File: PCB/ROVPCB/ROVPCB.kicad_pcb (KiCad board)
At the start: 2 copper layers, 65 x 56 mm, 17 parts, among them J1 Conn_01x04_Male, J2 Conn_01x04_Male, J3 Conn_Coaxial, P1 Conn_02x20_Odd_Even, U1 MPU-9250, U2 BME280, U3 LIGHT_TSL2591, U4 LTC4316IDDPBF, U5 AtlasOEM

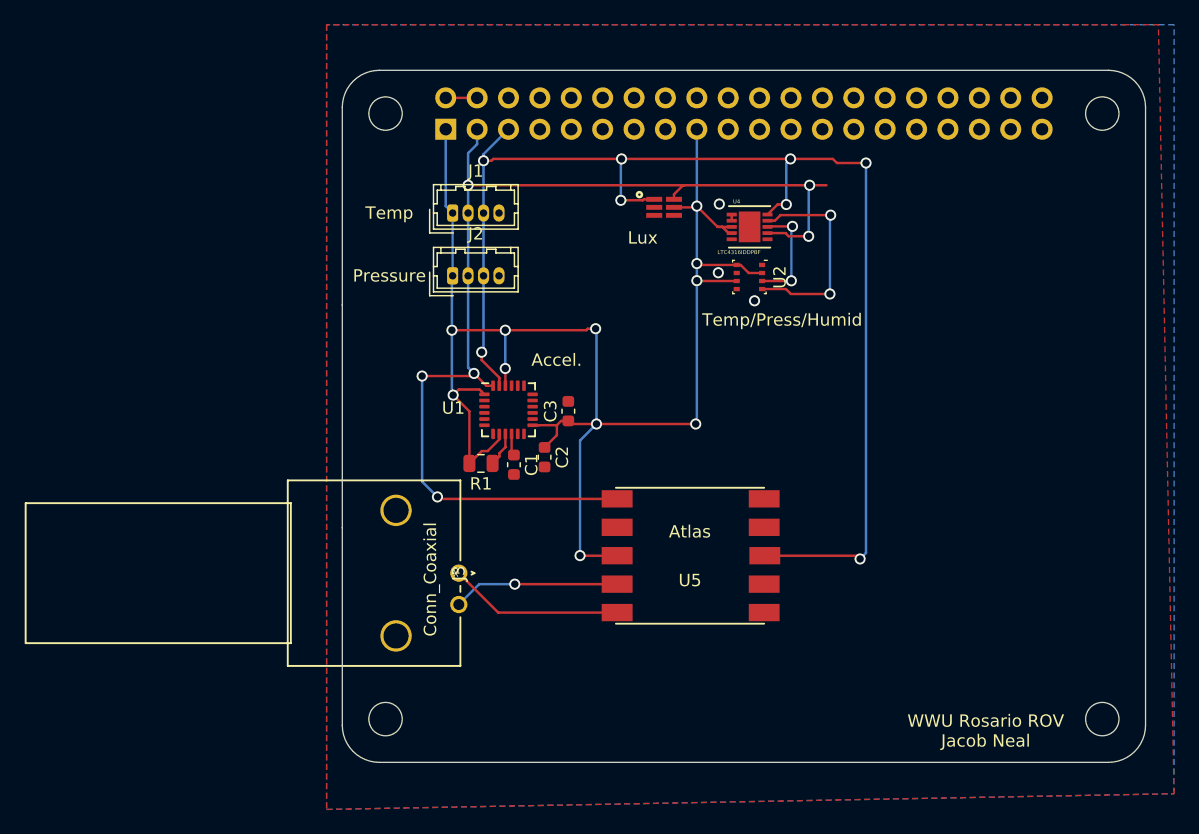
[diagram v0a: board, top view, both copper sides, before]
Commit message: NO BNC! YASSS
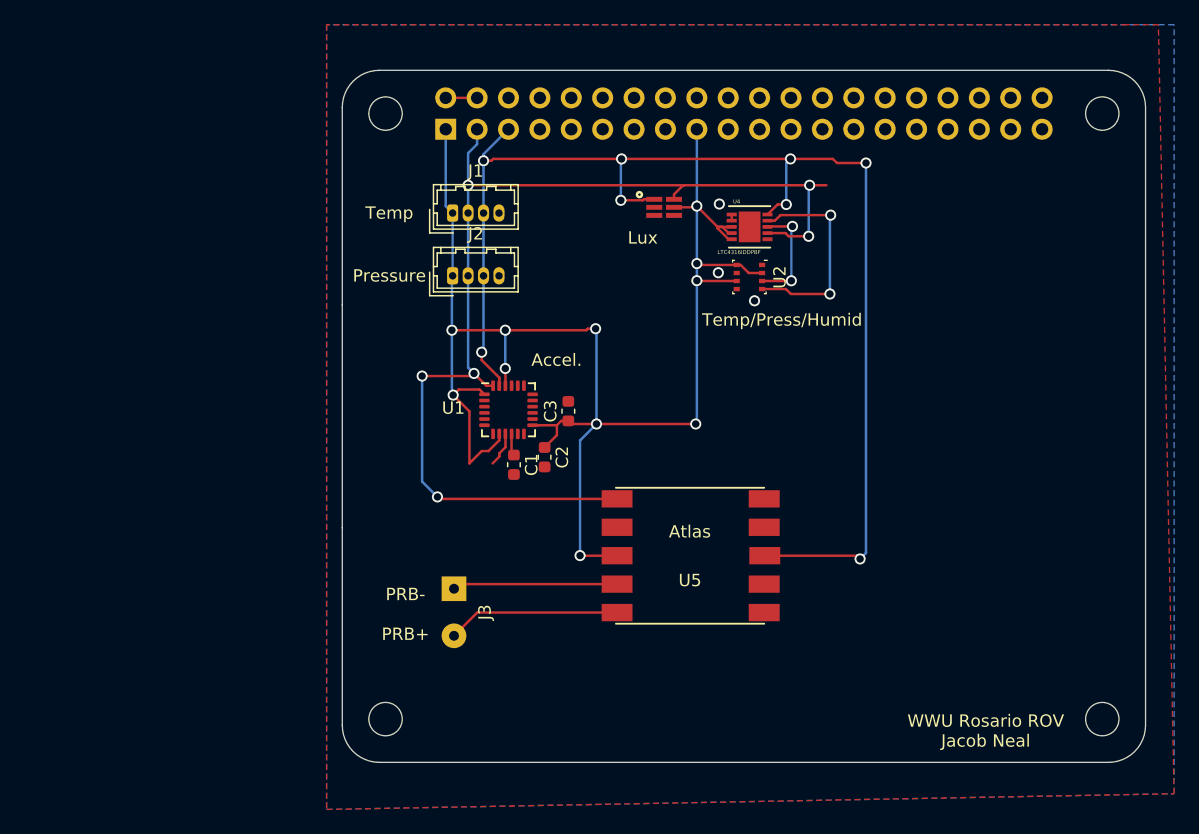
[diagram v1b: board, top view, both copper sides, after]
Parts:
- removed R1: 10k, Resistor_SMD:R_0805_2012Metric
- J3: value Conn_Coaxial -> Conn_01x02_Male; footprint footprints:5227161-1 -> Connector_Wire:SolderWirePad_1x02_P3.81mm_Drill0.8mm
- moved J3 1.32 mm to (209.0, 135.9), turned to 270 degrees
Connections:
- U1 pad 9: Net-(R1-Pad1) -> GND
- U4 pad 5: Net-(U4-Pad5) -> +3V3
- U5 pad 4: Net-(J3-Pad2) -> Net-(J3-Pad1)
- U5 pad 5: Net-(J3-Pad1) -> Net-(J3-Pad2)
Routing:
- net Net-(R1-Pad1): track 2.82 -> 0.00 mm
- net GND: track 0.50 -> 3.32 mm
- net +3V3: track 128.5 -> 130.1 mm
- net Net-(J3-Pad1): track 14.1 -> 13.4 mm
- net Net-(J3-Pad2): track 13.5 -> 14.0 mm, vias 1 -> 0
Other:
- board text added: "PRB- PRB+"

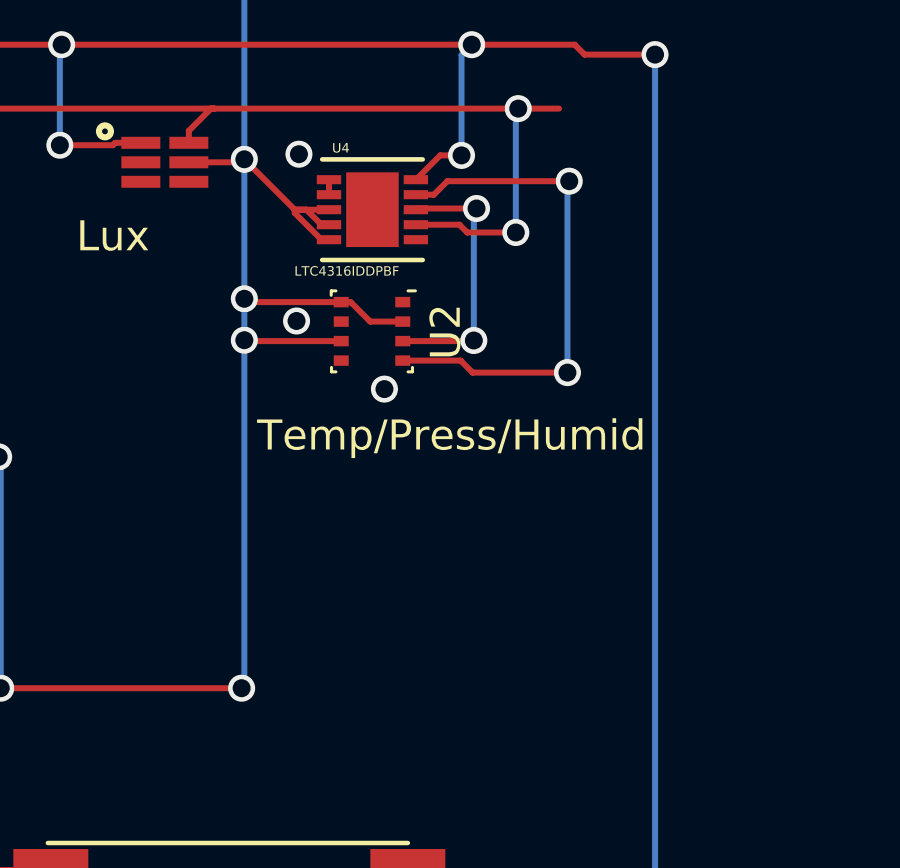
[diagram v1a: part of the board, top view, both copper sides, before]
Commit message: Pullup resistors in between translater and humidity sensor
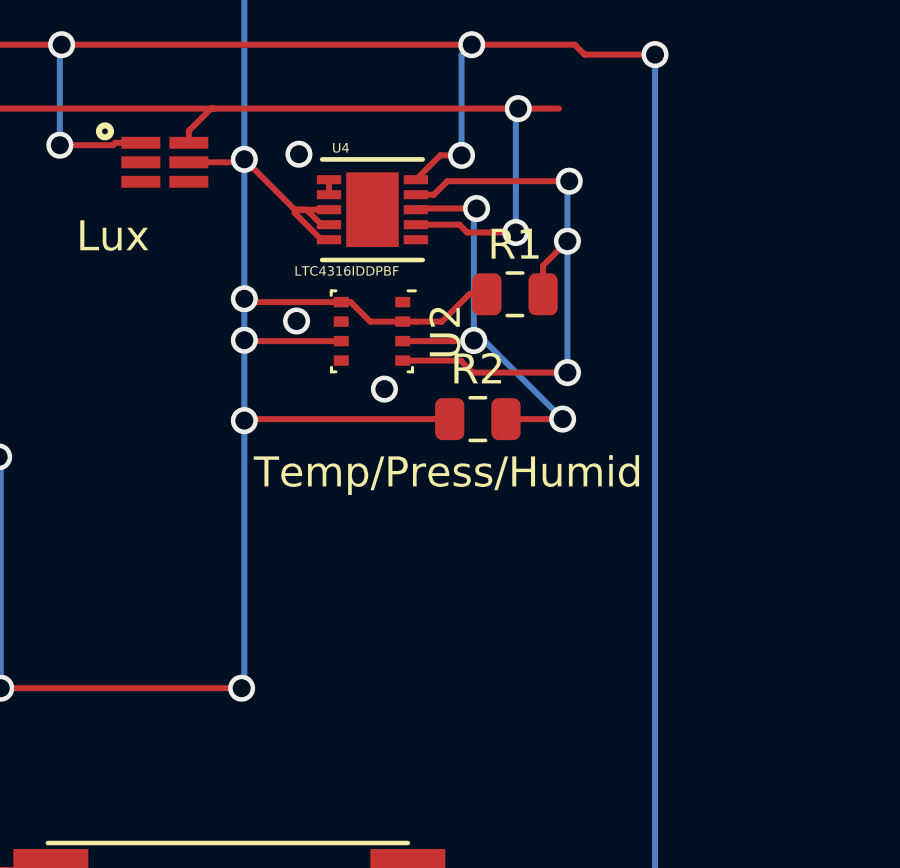
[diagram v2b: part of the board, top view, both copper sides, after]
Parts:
- added R1: 3k, Resistor_SMD:R_0805_2012Metric, F.Cu at (237.7, 109.5)
- added R2: 3k, Resistor_SMD:R_0805_2012Metric, F.Cu at (236.5, 113.7)
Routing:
- net +3V3: track 130.1 -> 140.2 mm, vias 11 -> 12
- net Net-(R2-Pad2): track 8.85 -> 14.8 mm, vias 2 -> 3
- net Net-(R1-Pad2): track 17.4 -> 19.5 mm, vias 2 -> 3

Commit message: I dont have time
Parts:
- added C4: 10uF, Capacitor_SMD:C_0603_1608Metric, F.Cu at (254.2, 113.7)
- added C5: 0.1uF, Capacitor_SMD:C_0603_1608Metric, F.Cu at (258.0, 110.1)
- added C6: 0.1uF, Capacitor_SMD:C_0603_1608Metric, F.Cu at (257.2, 113.2)
- added J4: Conn_01x01_Male, Connector_Wire:SolderWirePad_1x01_Drill0.8mm, F.Cu at (255.0, 110.9)
- added R3: 1k, Resistor_SMD:R_0805_2012Metric, F.Cu at (251.0, 113.9)
- added U6: LTC2451CTS8-TRMPBF, footprints:LTC2451CTS8-TRMPBF, F.Cu at (251.4, 111.1)
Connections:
- U5 pad 1: /GPIO2(SDA1) -> Net-(U5-Pad1)
- U5 pad 10: Net-(U5-Pad10) -> Net-(J3-Pad1)
- U5 pad 2: Net-(U5-Pad2) -> /GPIO3(SCL1)
- U5 pad 3: +3V3 -> Net-(U5-Pad3)
- U5 pad 4: Net-(J3-Pad1) -> Net-(U5-Pad4)
- U5 pad 5: Net-(J3-Pad2) -> Net-(U5-Pad5)
- U5 pad 6: GND -> Net-(U5-Pad6)
- U5 pad 7: Net-(U5-Pad7) -> /GPIO2(SDA1)
- U5 pad 8: /GPIO3(SCL1) -> Net-(U5-Pad8)
- U5 pad 9: Net-(U5-Pad9) -> +3V3

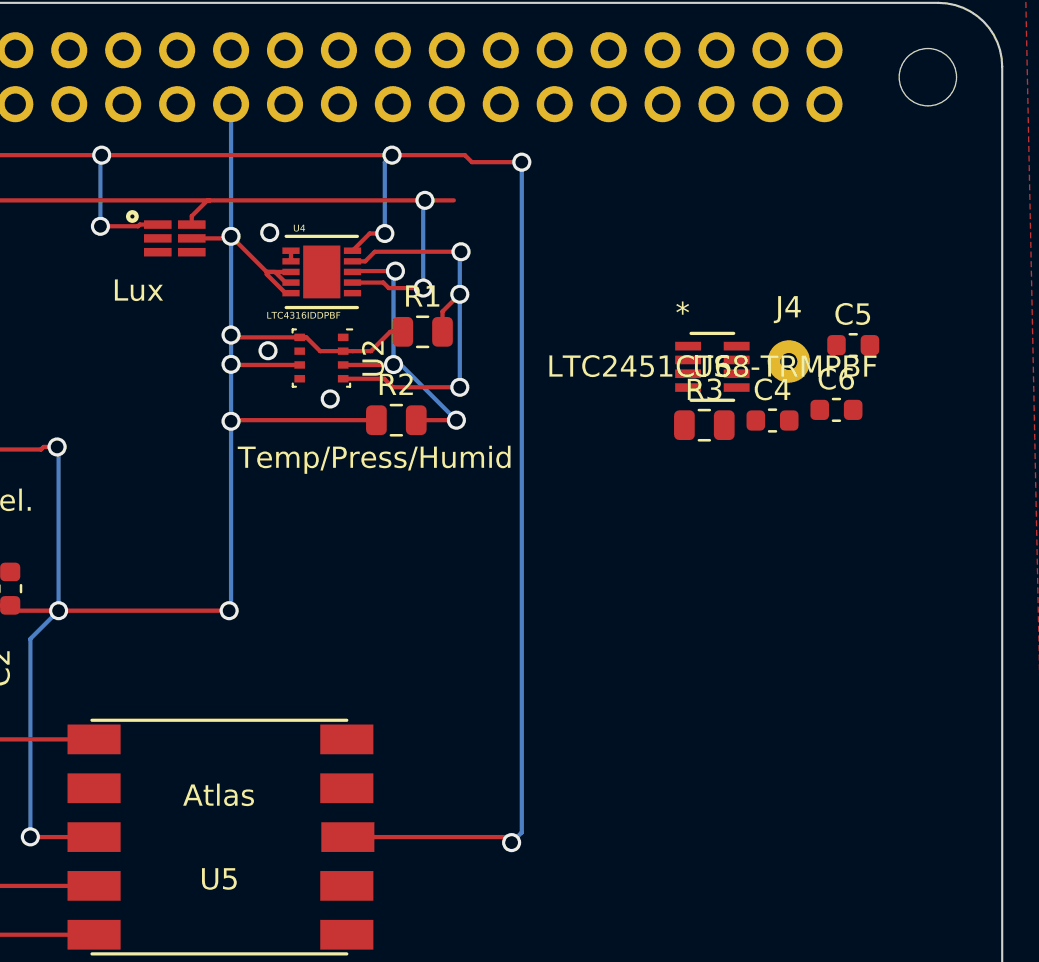
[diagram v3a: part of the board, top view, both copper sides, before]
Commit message: Fixed DRC errors and other things
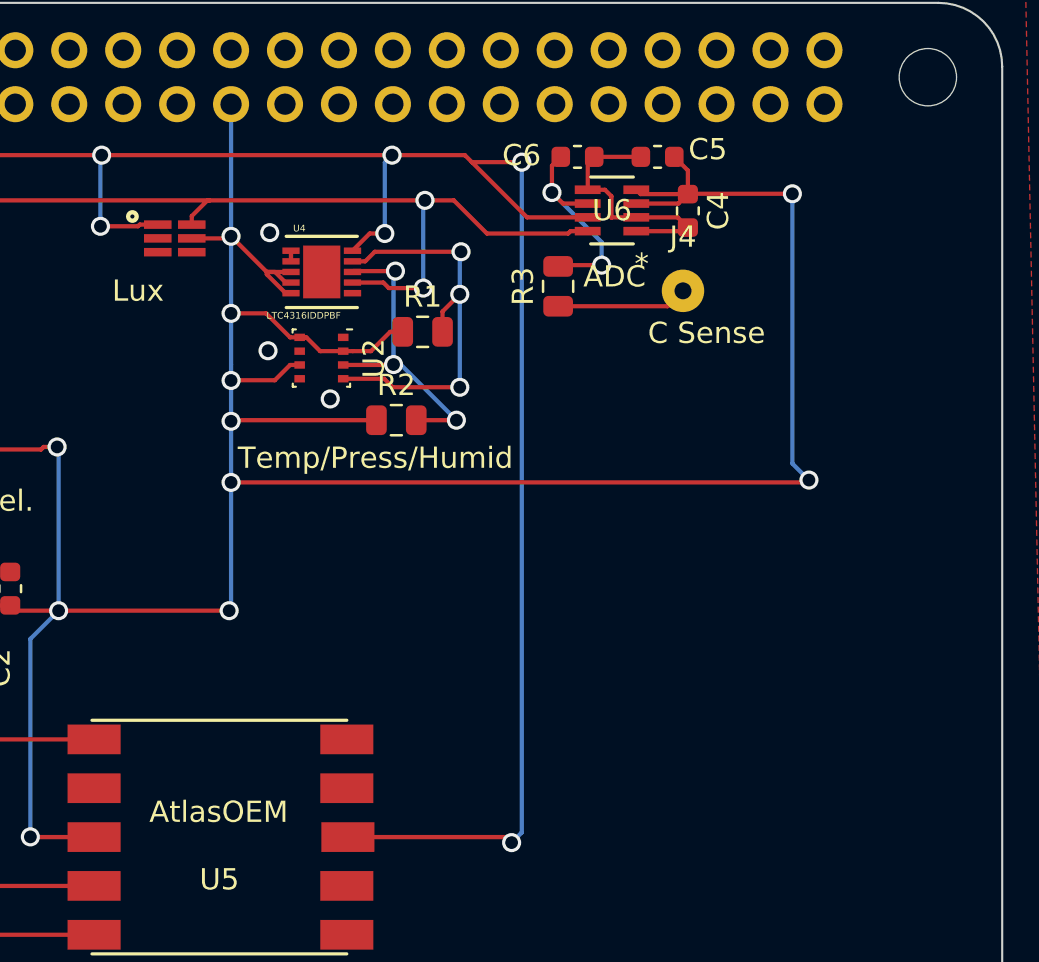
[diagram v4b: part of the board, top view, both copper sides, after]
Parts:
- U6: value LTC2451CTS8-TRMPBF -> ADC
- moved C6 17.0 mm to (245.0, 101.2)
- moved C5 12.8 mm to (248.8, 101.2), turned to 180 degrees
- moved C4 10.6 mm to (250.2, 103.8), turned to 270 degrees
- moved R3 9.49 mm to (244.1, 107.3), turned to 90 degrees
- moved U6 8.75 mm to (246.6, 103.8), turned to 180 degrees
- moved J4 5.99 mm to (250.0, 107.6)
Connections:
- U5 pad 1: Net-(U5-Pad1) -> /GPIO2(SDA1)
- U5 pad 10: Net-(J3-Pad1) -> Net-(U5-Pad10)
- U5 pad 2: /GPIO3(SCL1) -> Net-(U5-Pad2)
- U5 pad 3: Net-(U5-Pad3) -> +3V3
- U5 pad 4: Net-(U5-Pad4) -> Net-(J3-Pad1)
- U5 pad 5: Net-(U5-Pad5) -> Net-(J3-Pad2)
- U5 pad 6: Net-(U5-Pad6) -> GND
- U5 pad 7: /GPIO2(SDA1) -> Net-(U5-Pad7)
- U5 pad 8: Net-(U5-Pad8) -> /GPIO3(SCL1)
- U5 pad 9: +3V3 -> Net-(U5-Pad9)
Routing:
- net +3V3: track 140.2 -> 194.0 mm, vias 12 -> 15
- net GND: track 3.32 -> 15.7 mm
- net Net-(C6-Pad1): track 0.00 -> 10.2 mm, vias 0 -> 2
- net /GPIO2(SDA1): track 89.6 -> 96.6 mm
- net /GPIO3(SCL1): track 105.3 -> 111.8 mm
- net Net-(J4-Pad1): track 0.00 -> 6.18 mm
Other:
- board text added: "C Sense"
- board text removed: "Atlas"

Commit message: I think it is done!
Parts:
- U4: footprint LTC4316IDDPBF:DFN-10_DD -> Package_SO:MSOP-10_3x3mm_P0.5mm
- U6: value ADC -> LTC2451CTS8-TRMPBF
- moved U4 0.33 mm to (232.6, 106.7)
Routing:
- net +3V3: track 194.0 -> 190.3 mm, vias 15 -> 16
- net GND: vias 3 -> 2

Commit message: MAOR Changes
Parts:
- U6: value LTC2451CTS8-TRMPBF -> ADC
- moved C2 1.07 mm to (216.7, 126.3)
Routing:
- net +3V3: track 190.3 -> 191.2 mm
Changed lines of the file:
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@@
     (descr "Molex DF13 through hole, DF13-04P-1.25DSA, 4 Pins per row (https://www.hirose.com/product/en/products/DF13/DF13-2P-1.25DSA%2850%29/), generated with kicad-footprint-generator")
     (tags "connector Hirose  side entry")
-    (fp_text reference J1 (at 1.88 -3.4) (layer F.SilkS)
+    (fp_text reference J1 (at -5.03 -1.05) (layer F.SilkS)
       (effects (font (size 1 1) (thickness 0.15)))
     )
@@
     (descr "Molex DF13 through hole, DF13-04P-1.25DSA, 4 Pins per row (https://www.hirose.com/product/en/products/DF13/DF13-2P-1.25DSA%2850%29/), generated with kicad-footprint-generator")
     (tags "connector Hirose  side entry")
-    (fp_text reference J2 (at 1.88 -3.4) (layer F.SilkS)
+    (fp_text reference J2 (at -5.13 -1.13) (layer F.SilkS)
       (effects (font (size 1 1) (thickness 0.15)))
     )
@@
   )
   (module Capacitor_SMD:C_0603_1608Metric (layer F.Cu)
-    (at 216.37 125.3075 270)
+    (at 216.67 126.3375 270)
     (descr "Capacitor SMD 0603 (1608 Metric), square (rectangular) end terminal, IPC_7351 nominal, (Body size source: http://www.tortai-tech.com/upload/download/2011102023233369053.pdf), generated with kicad-footprint-generator")
     (tags capacitor)
@@
     (tags "lga land grid array")
     (attr smd)
-    (fp_text reference U2 (at 0.015 -2.465 270) (layer F.SilkS)
+    (fp_text reference U2 (at 2.475 0.045) (layer F.SilkS)
       (effects (font (size 1 1) (thickness 0.15)))
     )
@@
     (tags connector)
     (attr virtual)
-    (fp_text reference J4 (at 0 -2.54) (layer F.SilkS)
+    (fp_text reference J4 (at 0 -2.54) (layer F.SilkS) hide
       (effects (font (size 1 1) (thickness 0.15)))
     )
@@
   (module footprints:LTC2451CTS8-TRMPBF (layer F.Cu)
     (at 246.627 103.775001 180)
-    (fp_text reference U6 (at 0 0 180) (layer F.SilkS)
-      (effects (font (size 1 1) (thickness 0.15)))
-    )
-    (fp_text value LTC2451CTS8-TRMPBF (at -0.123 -3.114999 180) (layer F.SilkS)
+    (fp_text reference U6 (at 0.027 -2.624999 180) (layer F.SilkS)
+      (effects (font (size 1 1) (thickness 0.15)))
+    )
+    (fp_text value ADC (at 4.927 -0.124999 180) (layer F.SilkS)
       (effects (font (size 1 1) (thickness 0.15)))
     )
@@
     )
   )
+  (gr_line (start 200 131) (end 200 113) (layer Edge.Cuts) (width 0.1))
   (gr_text "C Sense" (at 251.08 109.55) (layer F.SilkS)
     (effects (font (size 1 1) (thickness 0.25)))
@@
     (effects (font (size 1 1) (thickness 0.25)))
   )
-  (gr_line (start 200 112.9795) (end 200 131.0135) (layer Edge.Cuts) (width 0.1))
   (gr_text "WWU Rosario ROV\nJacob Neal" (at 252.07 147.46) (layer F.SilkS)
     (effects (font (size 1 1) (thickness 0.25)))
@@
   (segment (start 228.69 122.53) (end 228.6 122.62) (width 0.2) (layer B.Cu) (net 1))
   (segment (start 218.54 122.62) (end 218.29 122.37) (width 0.2) (layer F.Cu) (net 1))
-  (segment (start 217.365 123.525) (end 216.37 124.52) (width 0.2) (layer F.Cu) (net 1))
-  (segment (start 217.365 122.72) (end 217.365 123.525) (width 0.2) (layer F.Cu) (net 1))
   (via (at 220.57 122.62) (size 0.9) (drill 0.6) (layers F.Cu B.Cu) (net 1))
   (segment (start 220.57 122.62) (end 218.54 122.62) (width 0.2) (layer F.Cu) (net 1))
@@
   (segment (start 228.69 104.99) (end 228.69 107.18) (width 0.2) (layer B.Cu) (net 1))
   (segment (start 228.69 107.18) (end 228.69 107.44) (width 0.2) (layer B.Cu) (net 1))
+  (segment (start 216.67 123.415) (end 217.365 122.72) (width 0.2) (layer F.Cu) (net 1))
+  (segment (start 216.67 125.55) (end 216.67 123.415) (width 0.2) (layer F.Cu) (net 1))
   (segment (start 208.37 96.23) (end 210.91 96.23) (width 0.2) (layer F.Cu) (net 2))
   (via (at 233.36 112.65) (size 0.9) (drill 0.6) (layers F.Cu B.Cu) (net 3))
@@
     (connect_pads (clearance 0.1))
     (min_thickness 0.1)
-    (fill yes (arc_segments 16) (thermal_gap 0.508) (thermal_bridge_width 0.508))
+    (fill (arc_segments 16) (thermal_gap 0.508) (thermal_bridge_width 0.508))
     (polygon
       (pts
@@
     (connect_pads (clearance 0.508))
     (min_thickness 0.254)
-    (fill yes (arc_segments 16) (thermal_gap 0.508) (thermal_bridge_width 0.508))
+    (fill (arc_segments 16) (thermal_gap 0.508) (thermal_bridge_width 0.508))
     (polygon
       (pts
